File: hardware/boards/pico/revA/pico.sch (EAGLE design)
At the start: 150 parts, among them IC2 TPS6300, J12 3.5mm TRRS Jack, J2 HIROSE_DM3BT-DSF-PEJSHIROSE_D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, J3 MOLEX_105450-0101MOLEX_105450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, Q2 ON_SEMI_MMBT5551LT1GON_SEMI_M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, U1 VS1053-L, U2 MICROCHIP_MCP73831T-2ATI-OTMI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, X3 FH12-45S-0.5SH

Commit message: housekeeping + checkpoint
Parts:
- added R56: 0Ω, rcl:R-US_R1206
- C1: value 50uF -> 50μF
- C13: value 0.1 uF -> 0.1μF
- C14, C6, C7: value 1uF -> 1μF
- C2: value .1uF -> 0.1μF
- C21, C23, C25, C33, C34, C38: value 0.1uF -> 0.1μF
- C22, C24, C26, C27: value 4.7uF -> 4.7μF
- C28, C29, C3, C32, C37, C4, C43: value 10uF -> 10μF
- C5: value 10 uF -> 10μF
- R1, R2, R26, R32, R4, R40, R41, R42, R43, R48, R49, R5, R50, R53, R6, R7: value 10k -> 10kΩ
- R10, R17, R18, R9: value 100k -> 100kΩ
- R11: value 10M -> 10MΩ
- R12: value 1M -> 1MΩ
- R13: value 10 -> 10Ω
- R14, R15: value 20 -> 20Ω
- R16: value 100K -> 100KΩ
- R19: value 155k -> 155kΩ
- R20: value 75k -> 75kΩ
- R21: value 35k -> 35kΩ
- R22: value 15k -> 15kΩ
- R23, R25, R33: value 5k -> 5kΩ
- R24, R45: value 50k -> 50kΩ
- R27, R28: value 5.1k -> 5.1kΩ
- R29: value 22.1k -> 22.1kΩ
- R3, R35: value 100 -> 100Ω
- R30: value 47.5k -> 47.5kΩ
- R31, R46, R47: value 1k -> 1kΩ
- R34: value 2k -> 2kΩ
- R36: value 50 -> 50Ω
- R37, R38, R39: value 4.7k -> 4.7kΩ
- R44: value 10K -> 10kΩ
- R51: value 180k -> 180kΩ
- R52: value 360k -> 360kΩ
- R54: value 315k -> 315kΩ
- R55: value 25 -> 25Ω
- R8: value 1.5K -> 1.5KΩ
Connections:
- net SYS_ENABLE: now also R56.2
- net VBAT: now also R56.1
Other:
- note added: "A backup, in case the power on/off circuitry does not behave as expected."
- moved on the sheet: C35, C5, TP2

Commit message: checkpoint: pico is trudging along
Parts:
- C30, C31: device rcl:C-USC0201 -> rcl:C-USC0402
- R56: device rcl:R-US_R1206 -> rcl:R-US_R0603
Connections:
- net CENTER_SW_PWR_TOP: now also CENTER_SW_PWR.1
- net GND: now also CENTER_SW_PWR.3
- net N$29: now also CENTER_SW.3
- net V3P3: now also CENTER_SW.1
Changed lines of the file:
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@@
 <part name="U$4" library="Crystal" deviceset="ECS12P88MHZ" device=""/>
 <part name="GND36" library="supply1" library_urn="urn:adsk.eagle:library:371" deviceset="GND" device=""/>
-<part name="C30" library="rcl" library_urn="urn:adsk.eagle:library:334" deviceset="C-US" device="C0201" package3d_urn="urn:adsk.eagle:package:23690/2" value="2.7pF"/>
-<part name="C31" library="rcl" library_urn="urn:adsk.eagle:library:334" deviceset="C-US" device="C0201" package3d_urn="urn:adsk.eagle:package:23690/2" value="4.7pF"/>
+<part name="C30" library="rcl" library_urn="urn:adsk.eagle:library:334" deviceset="C-US" device="C0402" package3d_urn="urn:adsk.eagle:package:23626/2" value="2.7pF"/>
+<part name="C31" library="rcl" library_urn="urn:adsk.eagle:library:334" deviceset="C-US" device="C0402" package3d_urn="urn:adsk.eagle:package:23626/2" value="4.7pF"/>
 <part name="U$7" library="L-0402" deviceset="L-0402" device="" value="1.6nH"/>
 <part name="GND37" library="supply1" library_urn="urn:adsk.eagle:library:371" deviceset="GND" device=""/>
@@
 <part name="R16" library="rcl" library_urn="urn:adsk.eagle:library:334" deviceset="R-US_" device="R0402" package3d_urn="urn:adsk.eagle:package:23547/3" value="100KΩ"/>
 <part name="R18" library="rcl" library_urn="urn:adsk.eagle:library:334" deviceset="R-US_" device="R0402" package3d_urn="urn:adsk.eagle:package:23547/3" value="100kΩ"/>
-<part name="R56" library="rcl" library_urn="urn:adsk.eagle:library:334" deviceset="R-US_" device="R1206" package3d_urn="urn:adsk.eagle:package:23540/2" value="0Ω"/>
+<part name="R56" library="rcl" library_urn="urn:adsk.eagle:library:334" deviceset="R-US_" device="R0603" package3d_urn="urn:adsk.eagle:package:23555/3" value="0Ω"/>
 </parts>
 <sheets>
@@
 <wire x1="40.64" y1="25.4" x2="35.56" y2="25.4" width="0.1524" layer="91"/>
 <junction x="40.64" y="25.4"/>
+<pinref part="CENTER_SW" gate="G$0" pin="1"/>
+<wire x1="66.04" y1="30.48" x2="71.12" y2="30.48" width="0.1524" layer="91"/>
+<junction x="71.12" y="30.48"/>
 </segment>
 </net>
@@
 <pinref part="GND31" gate="1" pin="GND"/>
 <wire x1="139.7" y1="12.7" x2="139.7" y2="10.16" width="0.1524" layer="91"/>
+<pinref part="CENTER_SW_PWR" gate="G$0" pin="3"/>
+<wire x1="144.78" y1="12.7" x2="139.7" y2="12.7" width="0.1524" layer="91"/>
+<junction x="139.7" y="12.7"/>
 </segment>
 </net>
@@
 <wire x1="139.7" y1="35.56" x2="170.18" y2="35.56" width="0.1524" layer="91"/>
 <label x="170.18" y="38.1" size="1.778" layer="95"/>
+<pinref part="CENTER_SW_PWR" gate="G$0" pin="1"/>
+<wire x1="144.78" y1="33.02" x2="139.7" y2="33.02" width="0.1524" layer="91"/>
+<junction x="139.7" y="33.02"/>
 </segment>
 </net>
@@
 <wire x1="73.66" y1="7.62" x2="73.66" y2="10.16" width="0.1524" layer="91"/>
 <junction x="73.66" y="10.16"/>
+<pinref part="CENTER_SW" gate="G$0" pin="3"/>
+<wire x1="66.04" y1="10.16" x2="71.12" y2="10.16" width="0.1524" layer="91"/>
+<junction x="71.12" y="10.16"/>
 </segment>
 </net>

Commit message: checkpoint: labels
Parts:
- renumbered J2 to MICRO_SD, U$7 to L3, X3 to DISPLAY_CONN
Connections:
- net GND: now also BATT_CON.1; no longer BATT_CON.3
- net VBAT: now also BATT_CON.3; no longer BATT_CON.1

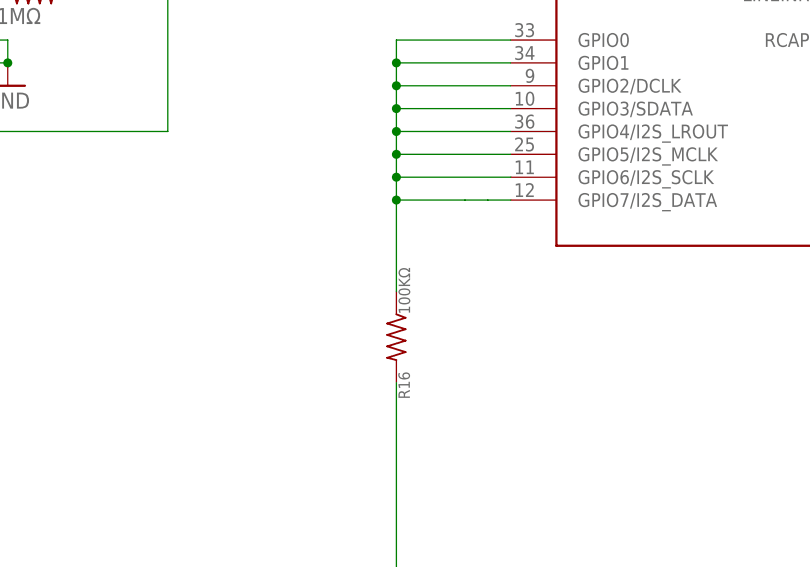
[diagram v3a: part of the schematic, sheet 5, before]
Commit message: pico: K -> k
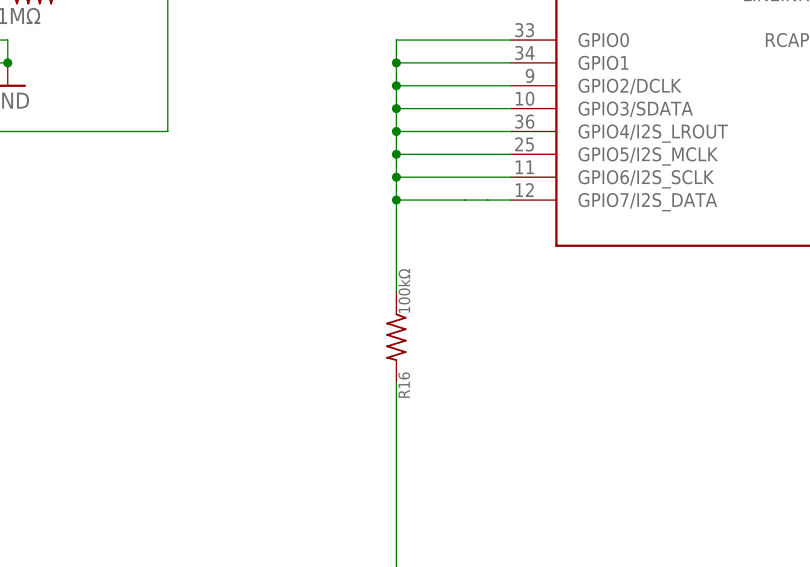
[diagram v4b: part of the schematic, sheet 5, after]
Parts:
- R16: value 100KΩ -> 100kΩ
- R8: value 1.5KΩ -> 1.5kΩ
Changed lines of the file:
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@@
 <part name="Q2" library="ON_Semi-MMBT5551LT1G" deviceset="ON_SEMI_MMBT5551LT1G" device="ON_SEMI_MMBT5551LT1G_0_0"/>
 <part name="D2" library="ON_Semi-1N914BWS" deviceset="ON_SEMI_1N914BWS" device="ON_SEMI_1N914BWS_0_0"/>
-<part name="R8" library="rcl" library_urn="urn:adsk.eagle:library:334" deviceset="R-US_" device="R0402" package3d_urn="urn:adsk.eagle:package:23547/3" value="1.5KΩ"/>
+<part name="R8" library="rcl" library_urn="urn:adsk.eagle:library:334" deviceset="R-US_" device="R0402" package3d_urn="urn:adsk.eagle:package:23547/3" value="1.5kΩ"/>
 <part name="IC2" library="texas" library_urn="urn:adsk.eagle:library:387" deviceset="TPS6300*" device="" package3d_urn="urn:adsk.eagle:package:7566968/1"/>
 <part name="R3" library="rcl" library_urn="urn:adsk.eagle:library:334" deviceset="R-US_" device="R0402" package3d_urn="urn:adsk.eagle:package:23547/3" value="100Ω"/>
@@
 <part name="C43" library="rcl" library_urn="urn:adsk.eagle:library:334" deviceset="C-US" device="C0402" package3d_urn="urn:adsk.eagle:package:23626/2" value="10μF"/>
 <part name="JP1" library="adafruit" library_urn="urn:adsk.eagle:library:420" deviceset="PINHD-1X8" device="LOCK" package3d_urn="urn:adsk.eagle:package:6240709/1"/>
-<part name="R16" library="rcl" library_urn="urn:adsk.eagle:library:334" deviceset="R-US_" device="R0402" package3d_urn="urn:adsk.eagle:package:23547/3" value="100KΩ"/>
+<part name="R16" library="rcl" library_urn="urn:adsk.eagle:library:334" deviceset="R-US_" device="R0402" package3d_urn="urn:adsk.eagle:package:23547/3" value="100kΩ"/>
 <part name="R18" library="rcl" library_urn="urn:adsk.eagle:library:334" deviceset="R-US_" device="R0402" package3d_urn="urn:adsk.eagle:package:23547/3" value="100kΩ"/>
 <part name="R56" library="rcl" library_urn="urn:adsk.eagle:library:334" deviceset="R-US_" device="R0603" package3d_urn="urn:adsk.eagle:package:23555/3" value="0Ω"/>
